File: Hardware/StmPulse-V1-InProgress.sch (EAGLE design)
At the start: 52 parts, among them IC1 78M05, IC2 MCP6004D, U1 MCP6004D, U2-MCP4922 MCP4922MCP4922-SO14

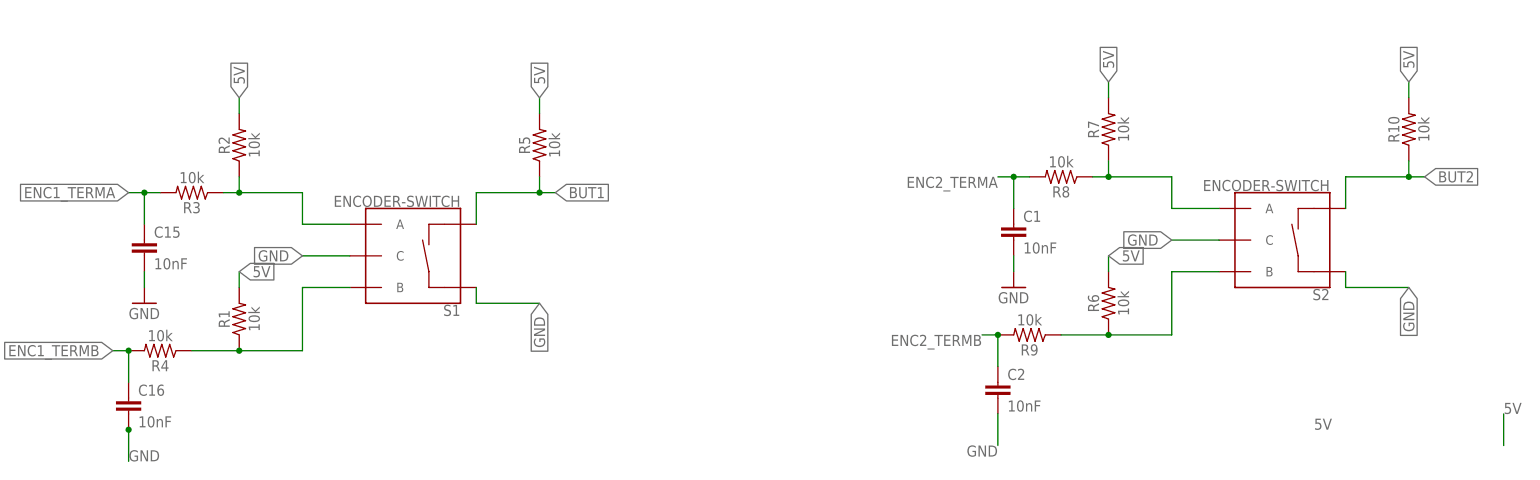
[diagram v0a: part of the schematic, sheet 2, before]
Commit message: Changed C and R to 805
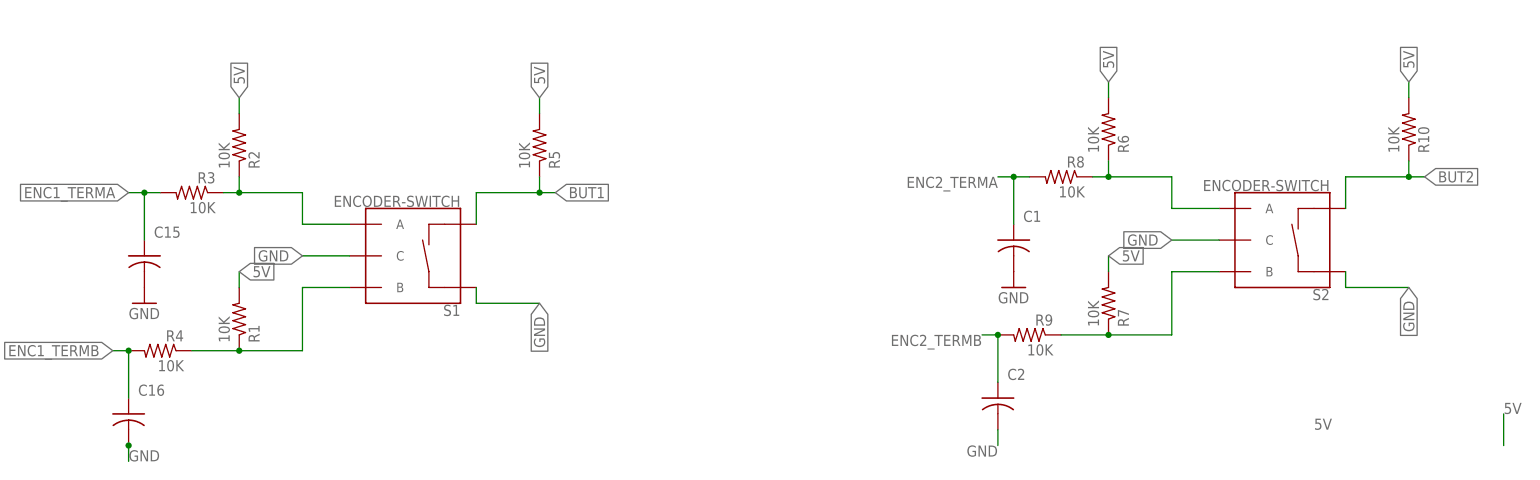
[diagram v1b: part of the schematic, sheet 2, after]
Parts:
- added CV3, CV4: S_JACK, INSTRUO:S_JACK
- C1, C15, C16, C2: device SparkFun-Capacitors:10NF-0603-50V-10% -> rcl:C-USC0805
- CLOCK1: value 2N3904 -> TRANSISTOR_MMBT3904
- R1, R10, R2, R3, R4, R5, R6, R7, R8, R9: value 10k -> 10K; device SparkFun-Resistors:10KOHM-0603-1/10W-1% -> rcl:R-US_R0805
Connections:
- new net N$4: CV3.TIP, U1A.-IN, U1A.OUT
- new net N$5: CV4.TIP, U1B.-IN, U1B.OUT
- net GND: now also CV3.GND, CV4.GND
- net N$1: now also R6.1; no longer R7.1
- net N$2: now also R7.1; no longer R6.1
- net VOUTA: now also U1A.+IN
- net VOUTB: now also U1B.+IN
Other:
- moved on the sheet: R3, R4, R6, R7, R8, R9

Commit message: Updated encoder switches
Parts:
- POWER: value HEADER2X5SHD -> (none); device GMSN:HEADER2X5SHD -> SparkFun-Connectors:CONN_05X2SHD_SMD
- PROGRAM: value (none) -> Program
- renumbered J1 to PROGRAM, JP1 to DISPLAY
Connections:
- net +5V: now also C6.1, C8.1, DISPLAY.2, R13.2
- net 5V: no longer C6.1, C8.1, DISPLAY.2, R13.2

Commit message: updated hardware
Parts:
- R14: value 330R -> 220R
- T1_CLOCK: LABLEL (none) -> T1_Start
- T2_RESET: LABEL (none) -> T2_Reset
- renumbered CLOCK to T1_CLOCK, CLOCK1 to T2_RESET
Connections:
- net BUTLED3: now also U$1.PA12; no longer U$1.PA11
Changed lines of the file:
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@@
 <part name="C3" library="rcl" deviceset="C-US" device="C0805K" value="100n"/>
 <part name="BUT3" library="INSTRUO" deviceset="PB6149L-5" device=""/>
-<part name="R14" library="rcl" deviceset="R-US_" device="R0805" value="330R"/>
+<part name="R14" library="rcl" deviceset="R-US_" device="R0805" value="220R"/>
 <part name="R23" library="rcl" deviceset="R-US_" device="R0805" value="100K"/>
-<part name="CLOCK" library="INSTRUO" deviceset="TRANSISTOR_MMBT3904" device="" value="2N3904">
+<part name="T1_CLOCK" library="INSTRUO" deviceset="TRANSISTOR_MMBT3904" device="" value="2N3904">
+<attribute name="LABLEL" value="T1_Start"/>
 <attribute name="RS-PART" value="725-8616 "/>
 </part>
@@
 <part name="R17" library="rcl" deviceset="R-US_" device="R0805" value="1M"/>
 <part name="START" library="INSTRUO" deviceset="S_JACK" device="" value="S_JACK"/>
-<part name="CLOCK1" library="INSTRUO" deviceset="TRANSISTOR_MMBT3904" device="" value="TRANSISTOR_MMBT3904">
+<part name="T2_RESET" library="INSTRUO" deviceset="TRANSISTOR_MMBT3904" device="" value="TRANSISTOR_MMBT3904">
+<attribute name="LABEL" value="T2_Reset"/>
 <attribute name="RS-PART" value="725-8616 "/>
 </part>
@@
 </segment>
 </net>
-<net name="BUTLED3" class="0">
-<segment>
-<pinref part="U$1" gate="G$1" pin="PA11"/>
-<wire x1="27.94" y1="66.04" x2="17.78" y2="66.04" width="0.1524" layer="91"/>
-<label x="17.78" y="66.04" size="1.778" layer="95" rot="R180"/>
-</segment>
-</net>
 <net name="START" class="0">
 <segment>
@@
 <wire x1="27.94" y1="83.82" x2="17.78" y2="83.82" width="0.1524" layer="91"/>
 <label x="17.78" y="83.82" size="1.778" layer="95" rot="R180"/>
+</segment>
+</net>
+<net name="BUTLED3" class="0">
+<segment>
+<pinref part="U$1" gate="G$1" pin="PA12"/>
+<wire x1="27.94" y1="63.5" x2="17.78" y2="63.5" width="0.1524" layer="91"/>
+<label x="17.78" y="63.5" size="1.778" layer="95" rot="R180"/>
 </segment>
 </net>
@@
 <attribute name="VALUE" x="154.178" y="123.19" size="1.778" layer="96" rot="MR90"/>
 </instance>
-<instance part="CLOCK" gate="G$1" x="5.08" y="190.5" smashed="yes" rot="R90">
+<instance part="T1_CLOCK" gate="G$1" x="5.08" y="190.5" smashed="yes" rot="R90">
 <attribute name="RS-PART" x="5.08" y="190.5" size="1.778" layer="96" rot="R90" display="off"/>
+<attribute name="LABLEL" x="5.08" y="190.5" size="1.778" layer="96" rot="R90"/>
 </instance>
 <instance part="R15" gate="G$1" x="10.16" y="213.36" smashed="yes" rot="MR90">
@@
 <attribute name="VALUE" x="-38.1" y="181.864" size="1.778" layer="96" rot="MR0"/>
 </instance>
-<instance part="CLOCK1" gate="G$1" x="142.24" y="185.42" smashed="yes" rot="R90">
+<instance part="T2_RESET" gate="G$1" x="142.24" y="185.42" smashed="yes" rot="R90">
 <attribute name="RS-PART" x="142.24" y="185.42" size="1.778" layer="96" rot="R90" display="off"/>
+<attribute name="LABEL" x="142.24" y="185.42" size="1.778" layer="96" rot="R90"/>
 </instance>
 <instance part="R18" gate="G$1" x="147.32" y="208.28" smashed="yes" rot="MR90">
@@
 </segment>
 <segment>
-<pinref part="CLOCK" gate="G$1" pin="E"/>
+<pinref part="T1_CLOCK" gate="G$1" pin="E"/>
 <wire x1="10.16" y1="177.8" x2="10.16" y2="175.26" width="0.1524" layer="91"/>
 <label x="10.16" y="175.26" size="1.778" layer="95"/>
@@
 </segment>
 <segment>
-<pinref part="CLOCK1" gate="G$1" pin="E"/>
+<pinref part="T2_RESET" gate="G$1" pin="E"/>
 <wire x1="147.32" y1="172.72" x2="147.32" y2="170.18" width="0.1524" layer="91"/>
 <label x="147.32" y="170.18" size="1.778" layer="95"/>
@@
 <net name="START" class="0">
 <segment>
-<pinref part="CLOCK" gate="G$1" pin="C"/>
+<pinref part="T1_CLOCK" gate="G$1" pin="C"/>
 <pinref part="R15" gate="G$1" pin="1"/>
 <wire x1="10.16" y1="208.28" x2="10.16" y2="205.74" width="0.1524" layer="91"/>
@@
 <wire x1="-17.78" y1="190.5" x2="-12.7" y2="190.5" width="0.1524" layer="91"/>
 <wire x1="-12.7" y1="190.5" x2="-12.7" y2="187.96" width="0.1524" layer="91"/>
-<pinref part="CLOCK" gate="G$1" pin="B"/>
+<pinref part="T1_CLOCK" gate="G$1" pin="B"/>
 <wire x1="-7.62" y1="190.5" x2="-12.7" y2="190.5" width="0.1524" layer="91"/>
 <junction x="-12.7" y="190.5"/>
@@
 <wire x1="119.38" y1="185.42" x2="124.46" y2="185.42" width="0.1524" layer="91"/>
 <wire x1="124.46" y1="185.42" x2="124.46" y2="182.88" width="0.1524" layer="91"/>
-<pinref part="CLOCK1" gate="G$1" pin="B"/>
+<pinref part="T2_RESET" gate="G$1" pin="B"/>
 <wire x1="129.54" y1="185.42" x2="124.46" y2="185.42" width="0.1524" layer="91"/>
 <junction x="124.46" y="185.42"/>
@@
 <net name="RESET" class="0">
 <segment>
-<pinref part="CLOCK1" gate="G$1" pin="C"/>
+<pinref part="T2_RESET" gate="G$1" pin="C"/>
 <pinref part="R18" gate="G$1" pin="1"/>
 <wire x1="147.32" y1="203.2" x2="147.32" y2="200.66" width="0.1524" layer="91"/>
